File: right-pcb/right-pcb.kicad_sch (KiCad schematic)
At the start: 78 parts, among them J3 BAT, U1 xiao-ble, U2 xiao-ble

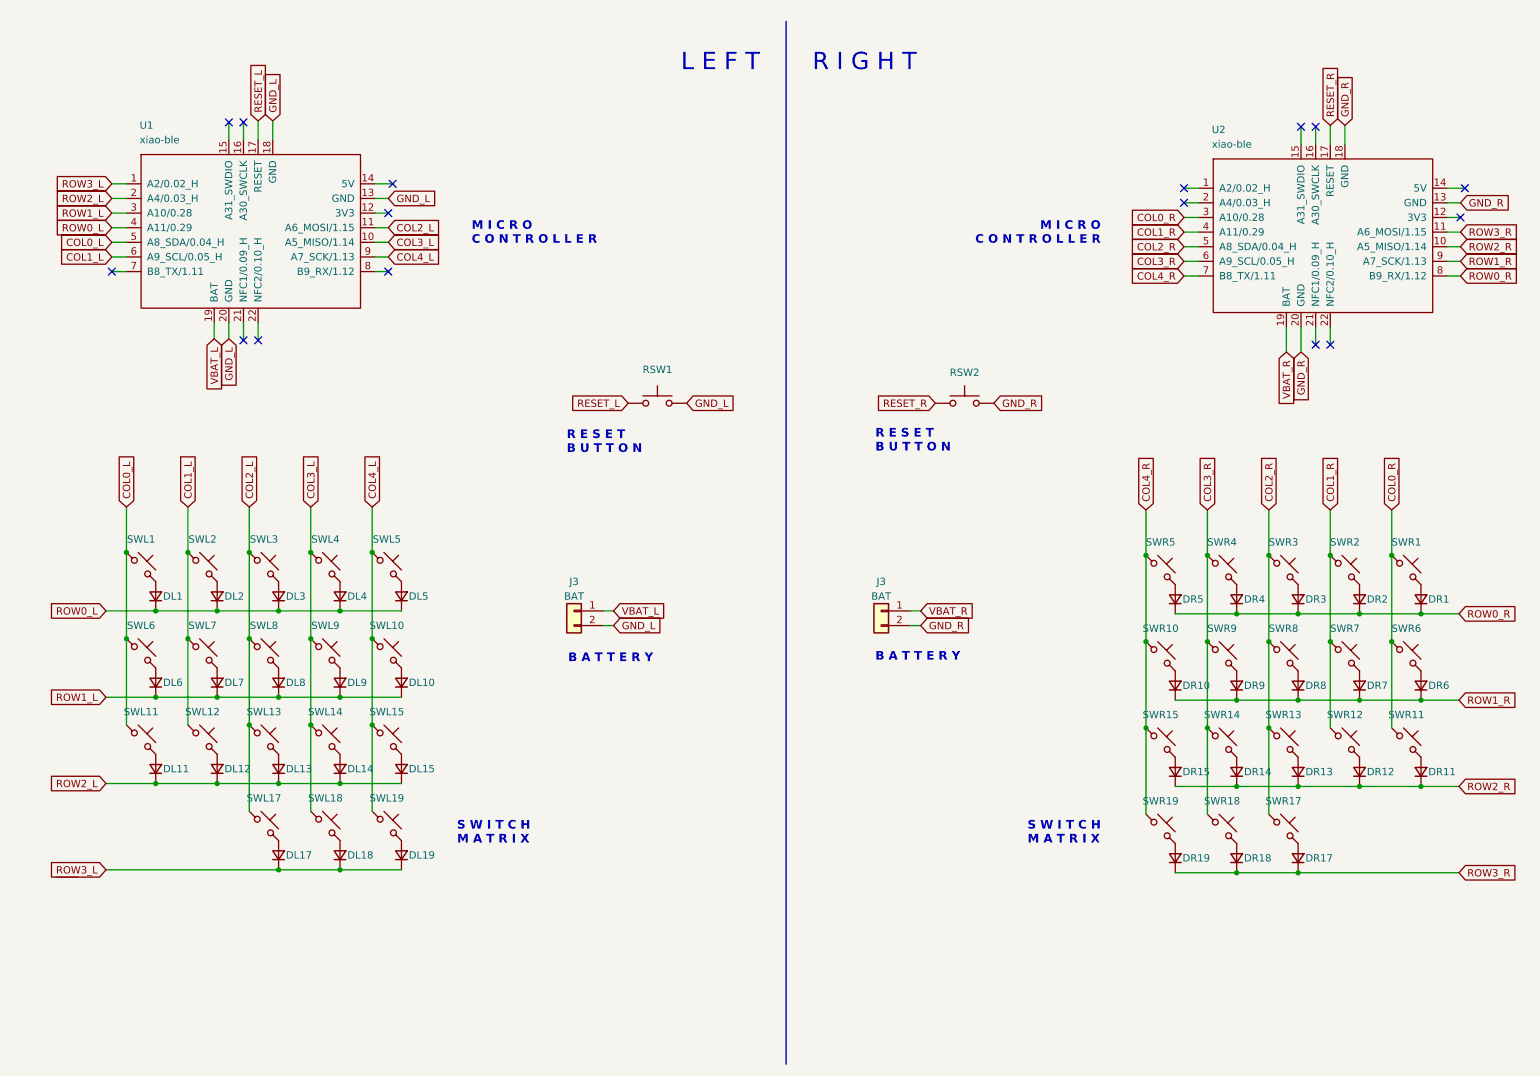
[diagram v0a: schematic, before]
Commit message: Update right-pcb schema to rev 0.3
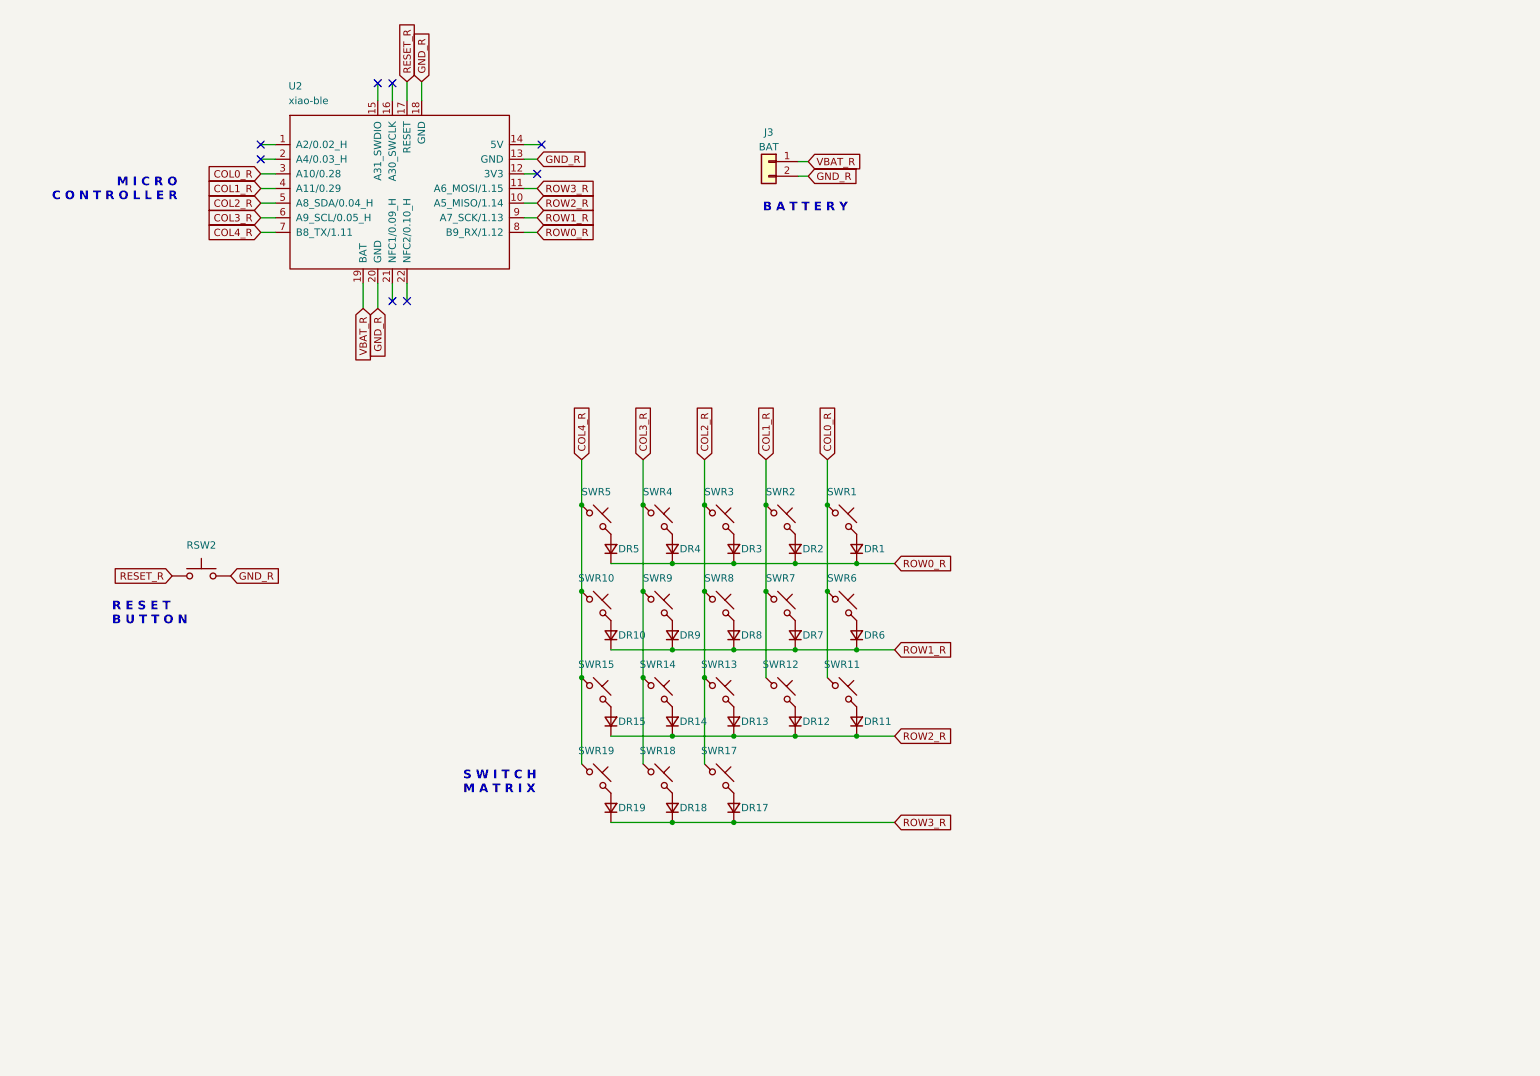
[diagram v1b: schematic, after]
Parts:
- removed DL1, DL10, DL11, DL12, DL13, DL14, DL15, DL17, DL18, DL19, DL2, DL3, DL4, DL5, DL6, DL7, DL8, DL9: D_Small, karmalib:Diode_SOD123, symbol Device:D_Small
- removed J3: BAT, Connector_JST:JST_PH_S2B-PH-SM4-TB_1x02-1MP_P2.00mm_Horizontal, symbol Connector_Generic:Conn_01x02
- removed RSW1: SW_Push, karmalib:SKHLLCA010, symbol Switch:SW_Push
- removed SWL1, SWL10, SWL11, SWL12, SWL13, SWL14, SWL15, SWL17, SWL18, SWL19, SWL2, SWL3, SWL4, SWL5, SWL6, SWL7, SWL8, SWL9: SW_Push_45deg, karmalib:Kailh_Socket_PG1350_Optional, symbol Switch:SW_Push_45deg
- removed U1: xiao-ble, karmalib:XIAO_nRF52840_SMD_Cutout, symbol mcu:xiao-ble
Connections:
- no-connect marks 16 -> 8
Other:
- note removed: "L E F T"
- note removed: "R I G H T"
- moved on the sheet: DR1, DR10, DR11, DR12, DR13, DR14, DR15, DR17, DR18, DR19, DR2, DR3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
